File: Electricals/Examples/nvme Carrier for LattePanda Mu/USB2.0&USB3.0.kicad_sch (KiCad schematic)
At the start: 13 parts, among them J2 USB_A_Stacked, J3 USB3_A, U3 ULC0524P, U4 ULC0524P

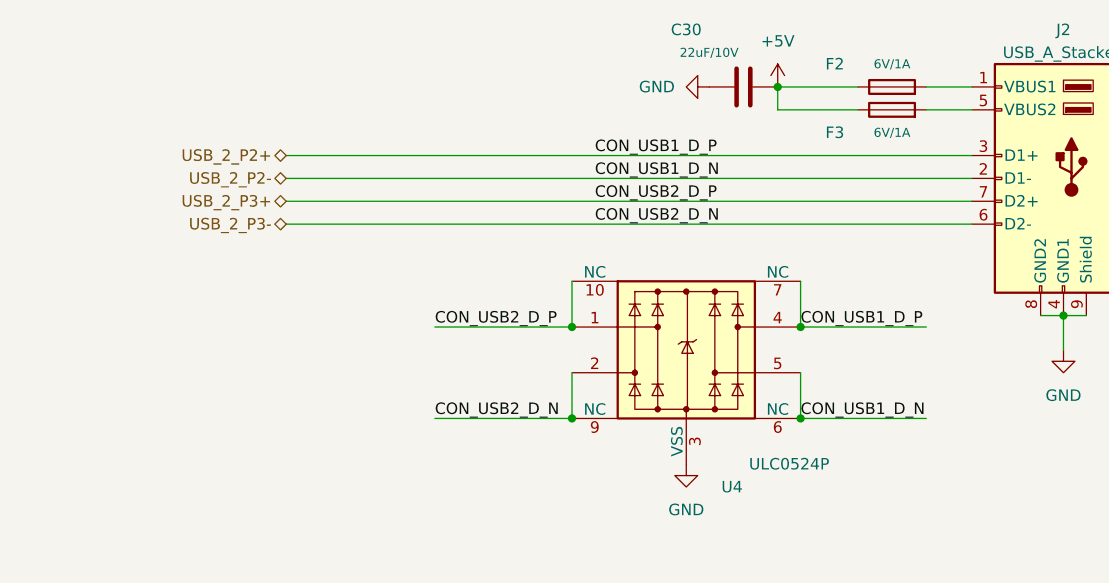
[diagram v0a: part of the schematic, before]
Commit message: Add BIOS Chip and small Changes to the Board
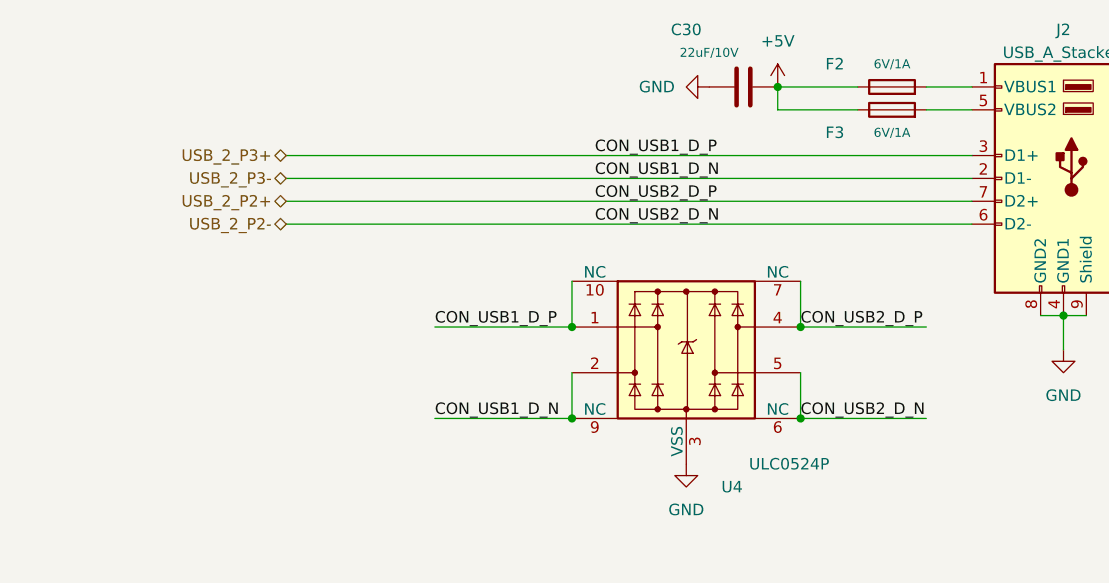
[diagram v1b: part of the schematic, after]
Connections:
- net USB_2_P2+: now also J2.7 (D2+); no longer J2.3 (D1+)
- net USB_2_P2-: now also J2.6 (D2-); no longer J2.2 (D1-)
- net USB_2_P3+: now also J2.3 (D1+); no longer J2.7 (D2+)
- net USB_2_P3-: now also J2.2 (D1-); no longer J2.6 (D2-)
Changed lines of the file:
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@@
 		)
 	)
-	(label "CON_USB1_D_N"
+	(label "CON_USB2_D_N"
 		(at 299.72 189.23 0)
 		(fields_autoplaced yes)
@@
 		)
 	)
-	(label "CON_USB2_D_P"
+	(label "CON_USB1_D_P"
 		(at 259.08 179.07 0)
 		(fields_autoplaced yes)
@@
 		)
 	)
-	(label "CON_USB1_D_P"
+	(label "CON_USB2_D_P"
 		(at 299.72 179.07 0)
 		(fields_autoplaced yes)
@@
 		)
 	)
-	(label "CON_USB2_D_N"
+	(label "CON_USB1_D_N"
 		(at 259.08 189.23 0)
 		(fields_autoplaced yes)
@@
 		)
 	)
-	(hierarchical_label "USB_2_P3+"
+	(hierarchical_label "USB_2_P2+"
 		(shape bidirectional)
 		(at 242.57 165.1 180)
@@
 		)
 	)
-	(hierarchical_label "USB_2_P2-"
+	(hierarchical_label "USB_2_P3-"
 		(shape bidirectional)
 		(at 242.57 162.56 180)
@@
 		)
 	)
-	(hierarchical_label "USB_2_P2+"
+	(hierarchical_label "USB_2_P3+"
 		(shape bidirectional)
 		(at 242.57 160.02 180)
@@
 		)
 	)
-	(hierarchical_label "USB_2_P3-"
+	(hierarchical_label "USB_2_P2-"
 		(shape bidirectional)
 		(at 242.57 167.64 180)

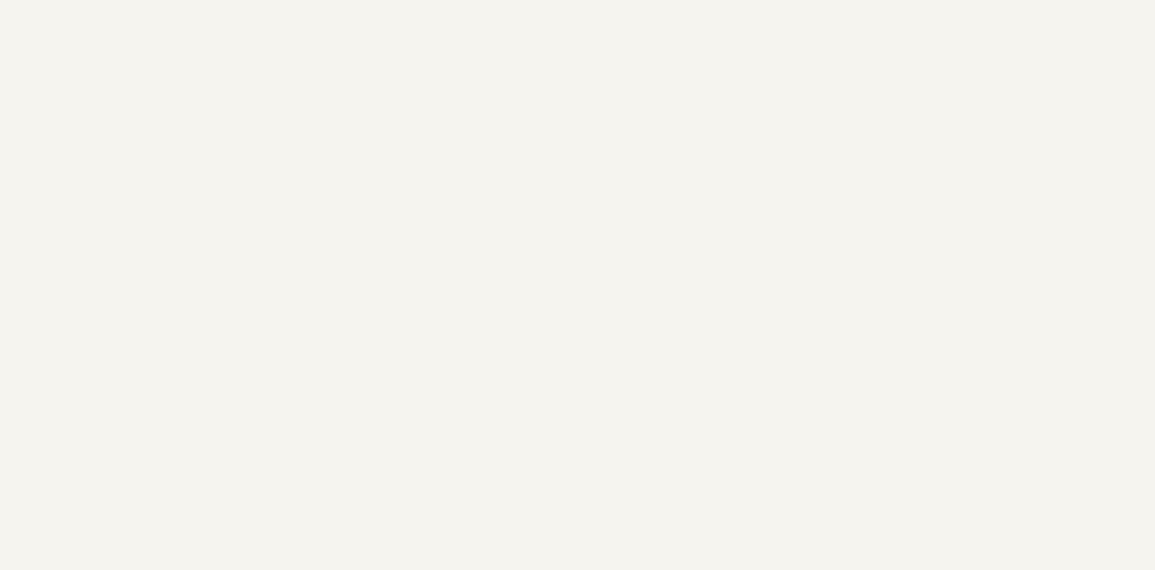
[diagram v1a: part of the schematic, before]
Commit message: Layout optimization + internal USB
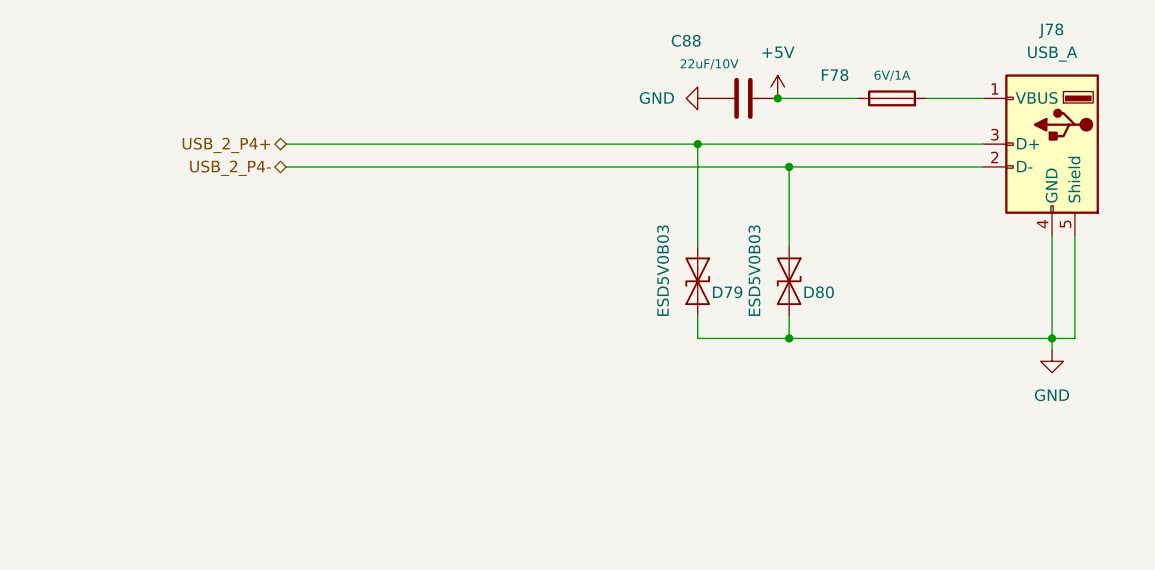
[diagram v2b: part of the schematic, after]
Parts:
- added C88: 22uF/10V, A_HDJ_Library:C_0603_1608Metric, symbol Device:C
- added D79, D80: ESD5V0B03, A_HDJ_Library:D_0402_1005Metric, symbol Diode:ESD9B5.0ST5G
- added F78: 6V/1A, A_HDJ_Library:Fuse_0805_2012Metric, symbol Device:Fuse
- added J78: USB_A, Connector_USB:USB_A_Molex_105057_Vertical, symbol Connector:USB_A
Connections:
- net +5V: now also C88.2, F78.1
- net GND: now also C88.1, D79.1 (A1), D80.1 (A1), J78.4 (GND), J78.5 (Shield)
- new net: F78.2, J78.1 (VBUS)
- new net USB_2_P4+: D79.2 (A2), J78.3 (D+)
- new net USB_2_P4-: D80.2 (A2), J78.2 (D-)
